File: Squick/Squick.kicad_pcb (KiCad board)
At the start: 2 copper layers, 92 x 92 mm, 103 parts, among them J1 BT, J10 D24V3F-5V, J2 DEBUG_UART, J3 PROG, J4 VL53L0X_L, J5 VL53L0X_F, J6 VL53L0X_R, J7 ENK_L, J8 ENK_R, J9 BATT, Q1 AO3407A, Q2 AO3407A, SW1 USER_BUT_1, SW2 USER_BUT_2, SW3 RESET, SW4 ON/OFF, T1 SFH-313FA, T2 SFH-313FA, T3 SFH-313FA, T4 SFH-313FA, T5 SFH-313FA, T6 SFH-313FA, U1 STM32F411RETx, U10 LM1117-3.3, U2 CD4051B, U3 KTIR0711S, U4 CD4051B, U5 KTIR0711S, U6 KTIR0711S, U7 KTIR0711S, U8 Adafruit_4554, U9 TB6612FNG

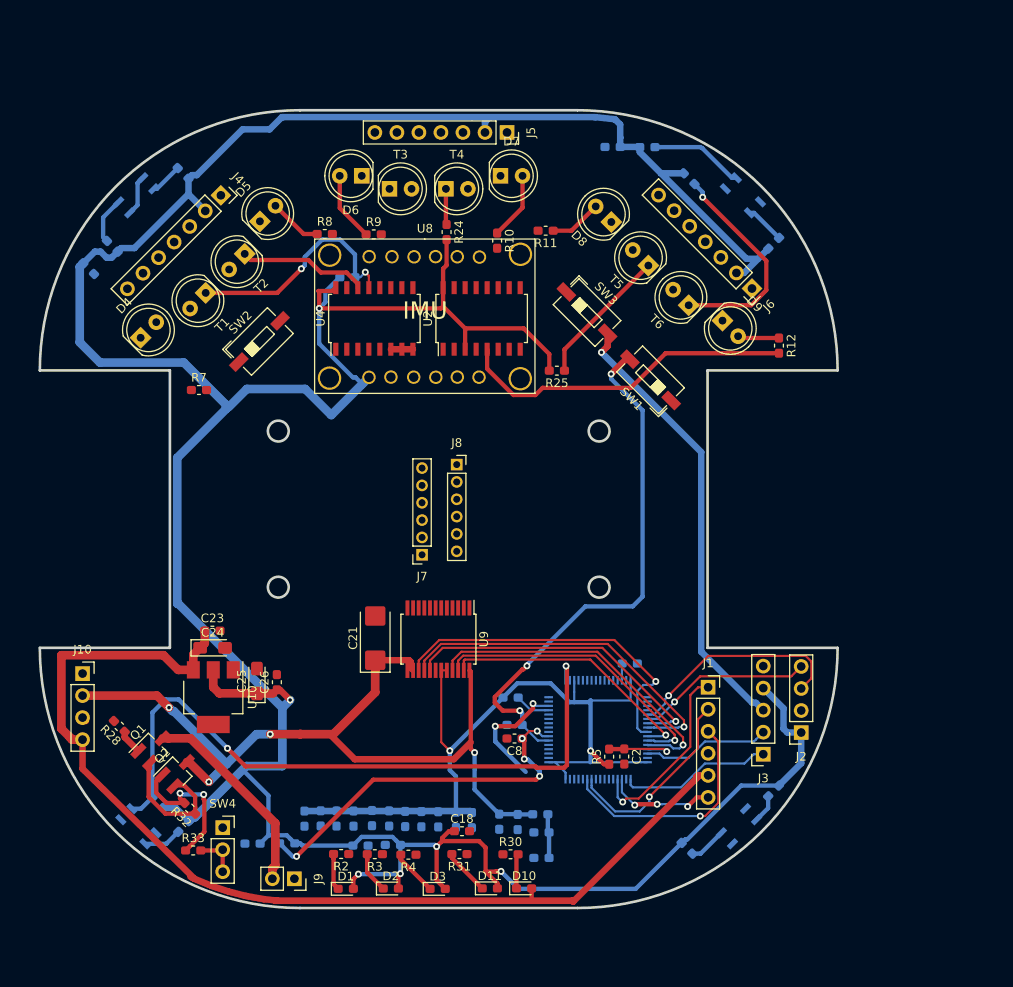
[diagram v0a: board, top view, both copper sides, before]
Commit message: Optimalization of connections and some reorganizations. Light in the tunnel
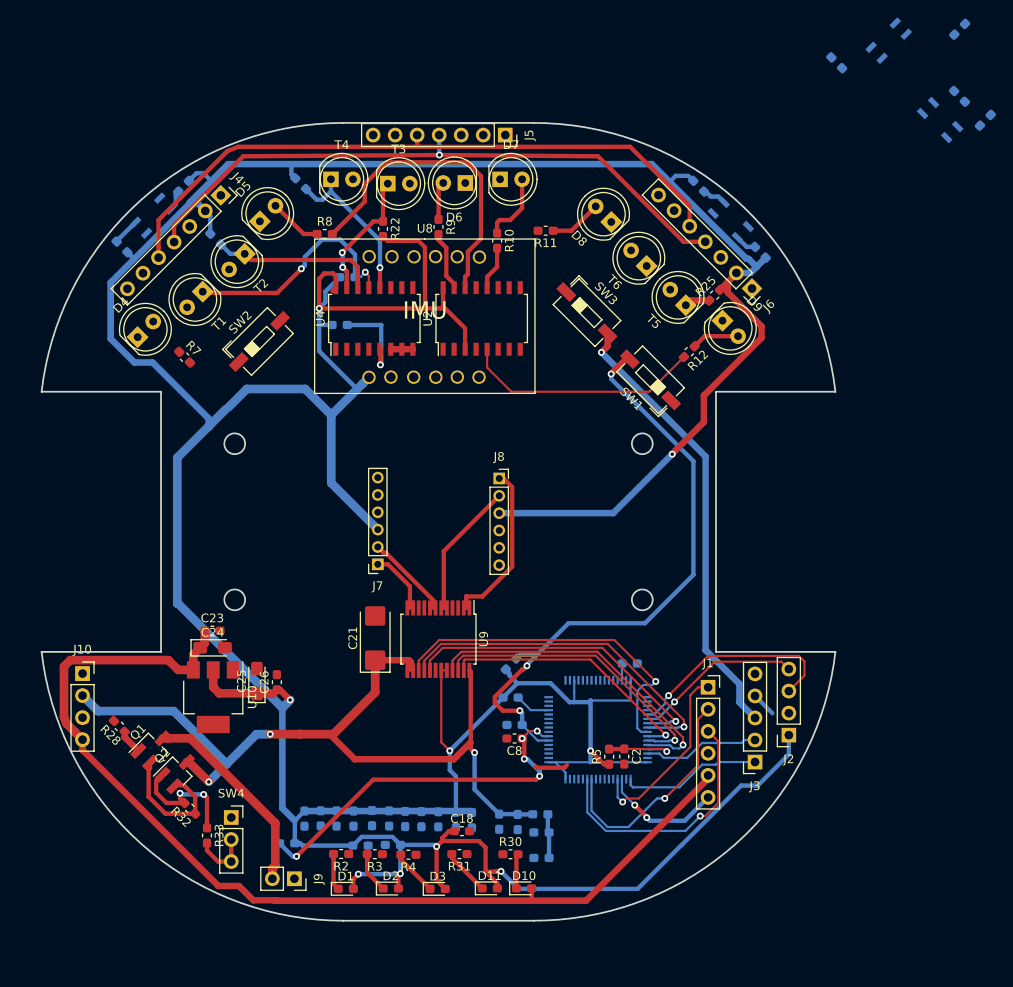
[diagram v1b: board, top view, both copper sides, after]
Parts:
- R22: moved to F.Cu
- R24: moved to B.Cu
- moved R18 123.2 mm to (243.2, 35.1)
- moved R19 123.2 mm to (240.2, 32.3)
- moved U6 123.2 mm to (237.9, 35.1)
- moved R23 92.2 mm to (226.0, 28.5)
- moved U7 92.2 mm to (232.0, 25.9)
- moved R21 90.4 mm to (240.2, 24.6)
- moved R26 43.7 mm to (168.7, 58.7), turned to 180 degrees
- moved R1 36.3 mm to (188.5, 97.8), turned to 45 degrees
- moved R22 28.1 mm to (173.7, 47.6), turned to 270 degrees
- moved R25 20.2 mm to (211.9, 55.3), turned to 45 degrees
- moved R24 17.7 mm to (164.2, 42.4), turned to 135 degrees
- moved R20 15.0 mm to (154.4, 48.8)
- moved T4 13.3 mm to (167.7, 41.9)
- moved D6 12.0 mm to (183.2, 42.3)
- moved R12 10.4 mm to (209.0, 61.8), turned to 225 degrees
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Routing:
- net SCL: track 0.00 -> 75.6 mm
- net KTIR_3: track 77.6 -> 3.82 mm, vias 2 -> 0
- net SDA: track 0.00 -> 72.9 mm, vias 0 -> 1
- net IR_2: track 0.00 -> 36.0 mm
- net +3.3V: track 512.5 -> 534.5 mm, vias 8 -> 9
- net M1_R: track 0.00 -> 19.8 mm
- net +5V: track 167.3 -> 148.0 mm
- net M2_R: track 0.00 -> 16.2 mm
- net PT_3: track 0.00 -> 15.3 mm, vias 0 -> 2
- net PT_4: track 4.14 -> 19.1 mm, vias 0 -> 1
- net PT_6: track 25.3 -> 10.4 mm
- net V_batt: track 19.5 -> 5.09 mm, vias 2 -> 0
- net PT_5: track 16.1 -> 2.93 mm
- net IR_6: track 39.6 -> 28.1 mm
- net M2_L: track 0.00 -> 10.5 mm
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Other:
- board size 92 x 92 mm -> 91.5 x 92 mm

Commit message: Almost finished. It's getting really tight
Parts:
- C8: moved to B.Cu
- moved C19 23.1 mm to (164.5, 110.9)
- moved C20 23.1 mm to (166.7, 110.9)
- moved R29 23.1 mm to (169.4, 112.1)
- moved R27 23.1 mm to (169.3, 110.0)
- moved C22 20.6 mm to (173.0, 112.1), turned to 180 degrees
- moved C23 3.23 mm to (150.8, 94.0)
- moved C1 2.14 mm to (188.7, 107.0)
- moved C24 1.85 mm to (152.2, 95.8)
- moved D6 1.25 mm to (183.9, 43.3)
- moved D7 1.25 mm to (187.9, 42.9)
- moved T3 1.25 mm to (175.0, 43.4)
- moved T4 1.25 mm to (168.4, 42.9)
- moved J10 1.01 mm to (139.9, 99.5)
- moved C8 0.96 mm to (188.7, 105.5)
- moved R24 0.81 mm to (163.9, 43.1)
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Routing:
- net MISO: track 0.24 -> 104.4 mm, vias 0 -> 2
- net IMU_CS: track 0.00 -> 103.0 mm, vias 0 -> 2
- net IR_A: track 0.00 -> 83.9 mm, vias 0 -> 3
- net IR_B: track 0.00 -> 79.2 mm, vias 0 -> 3
- net SCK: track 0.28 -> 77.7 mm, vias 0 -> 4
- net IMU_INT: track 0.00 -> 75.8 mm, vias 0 -> 2
- net VL_XSHUT: track 0.00 -> 75.6 mm, vias 0 -> 2
- net IR_C: track 0.00 -> 73.4 mm, vias 0 -> 3
- net MOSI: track 0.00 -> 70.6 mm, vias 0 -> 2
- net BUT_2: track 9.10 -> 75.7 mm, vias 1 -> 3
- net VL_INT_R: track 0.00 -> 64.6 mm, vias 0 -> 3
- net +3.3V: track 534.5 -> 587.1 mm, vias 9 -> 10
- net IR_1: track 0.00 -> 37.2 mm
- net +5V: track 148.0 -> 121.2 mm
- net BT_RX: track 26.6 -> 47.1 mm
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
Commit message: Everything connected
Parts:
- moved R18 79.5 mm to (163.8, 38.9), turned to 45 degrees
- moved U6 69.5 mm to (168.5, 38.8), turned to 270 degrees
- moved R19 66.4 mm to (174.1, 39.4), turned to 0 degrees
- moved R21 54.2 mm to (187.9, 38.6), turned to 0 degrees
- moved U7 41.7 mm to (192.3, 38.5), turned to 270 degrees
- moved R1 41.5 mm to (206.3, 60.3), turned to 135 degrees
- moved R23 30.5 mm to (197.5, 39.4), turned to 0 degrees
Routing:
- net KTIR_3: track 0.00 -> 145.4 mm, vias 0 -> 10
- net VL_INT_L: track 0.05 -> 112.9 mm, vias 0 -> 5
- net SDA: track 73.1 -> 182.8 mm, vias 1 -> 9
- net KTIR_4: track 0.00 -> 107.0 mm, vias 0 -> 4
- net VL_INT_F: track 0.00 -> 99.4 mm, vias 0 -> 8
- net SCL: track 75.8 -> 170.2 mm, vias 0 -> 6
- net LED_2: track 0.00 -> 80.2 mm, vias 0 -> 5
- net PT_MEAS: track 0.00 -> 79.1 mm, vias 0 -> 3
- net PT_A: track 5.42 -> 77.8 mm, vias 2 -> 5
- net PT_B: track 0.00 -> 66.2 mm, vias 0 -> 5
- net PT_C: track 0.00 -> 63.5 mm, vias 0 -> 5
- net PT_5: track 2.93 -> 64.8 mm, vias 0 -> 2
- net LED_3: track 0.00 -> 60.7 mm, vias 0 -> 3
- net LED_1: track 0.00 -> 58.4 mm, vias 0 -> 4
- net BUT_2: track 75.7 -> 126.9 mm, vias 3 -> 9
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
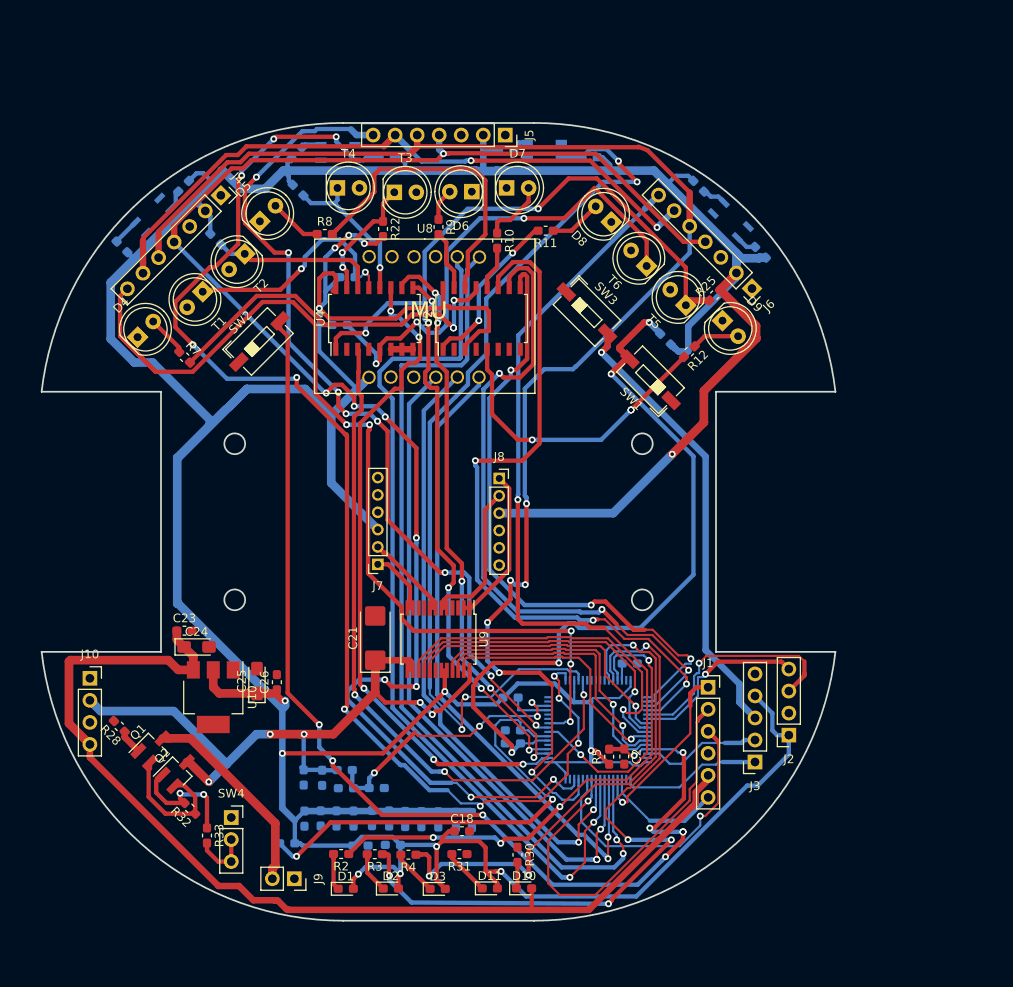
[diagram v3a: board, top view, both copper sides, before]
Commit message: Improved via drills and added graphic symbols
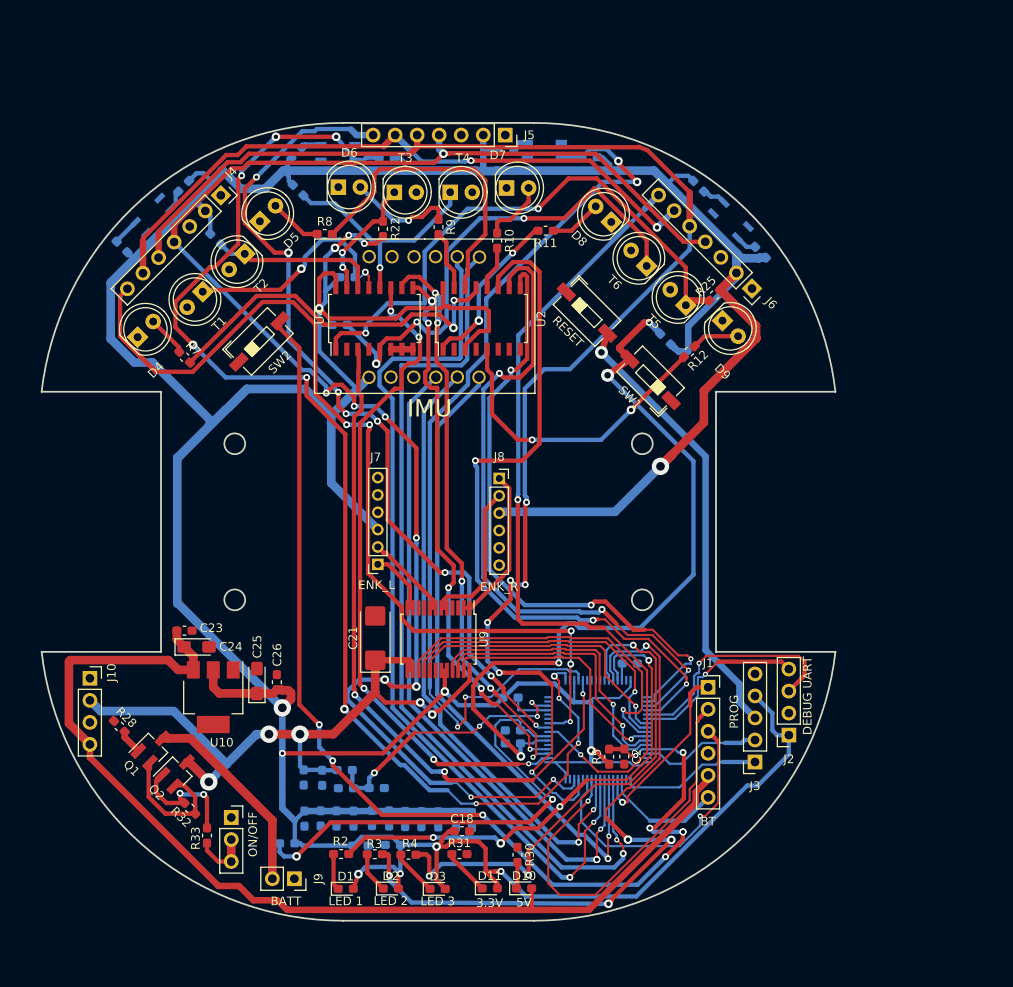
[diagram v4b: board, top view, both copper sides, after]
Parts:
- added G***: LOGO, graphics:Mouse_20x20mm, B.Cu at (163.8, 81.3)
- D1: value LED_1 -> LED 1
- D10: value LED_5V -> 5V
- D11: value LED_3.3V -> 3.3V
- D2: value LED_2 -> LED 2
- D3: value LED_3 -> LED 3
- J2: value DEBUG_UART -> DEBUG UART
- moved D6 15.4 mm to (168.6, 42.8), turned to 0 degrees
- moved T4 13.0 mm to (181.4, 43.4)
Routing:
- net PT_4: track 18.8 -> 28.1 mm
- net Net-(D6-Pad2): track 3.74 -> 12.5 mm, vias 0 -> 1
- net +3.3V: track 607.8 -> 613.8 mm
- net IR_1: track 43.6 -> 45.2 mm, vias 3 -> 2
- net BUT_1: track 86.1 -> 87.6 mm
- net Vin: track 77.7 -> 79.0 mm
- net PT_6: track 57.9 -> 59.1 mm
- net V_batt: track 31.9 -> 32.6 mm
- net KTIR_4: track 107.0 -> 106.5 mm
- net IR_6: vias 3 -> 2
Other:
- board text added: "Patryk Szydlik"
- board text added: "Piotr Gorzelnik"
- board text added: "Squick"

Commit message: Made more space for BT module and 5V converter
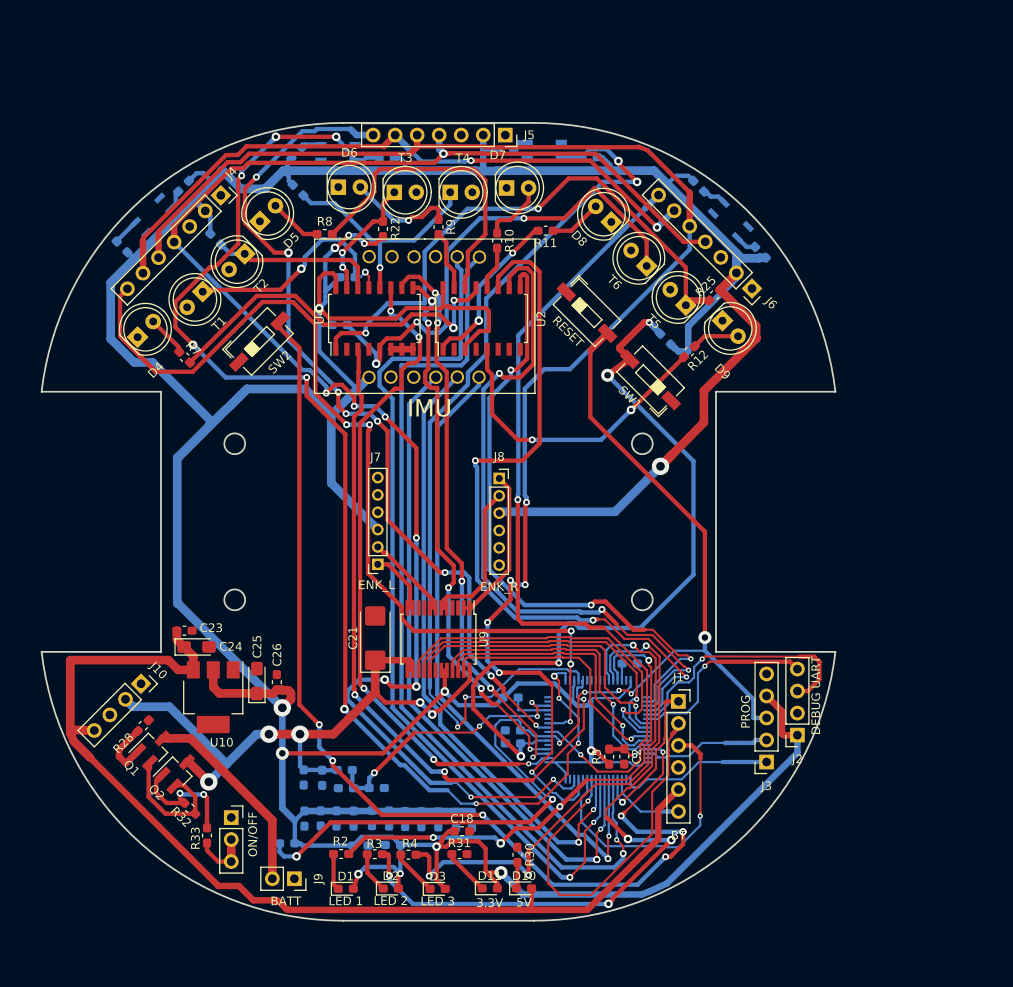
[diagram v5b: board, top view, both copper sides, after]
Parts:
- moved J10 5.93 mm to (145.8, 100.1), turned to 315 degrees
- moved G*** 5.10 mm to (159.0, 79.8), turned to 180 degrees
- moved J1 3.79 mm to (207.8, 102.1)
- moved R28 2.76 mm to (146.1, 104.9), turned to 45 degrees
- moved J3 1.33 mm to (217.9, 109.1)
- moved J2 0.99 mm to (221.5, 106.0)
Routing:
- net RESET: track 106.4 -> 134.3 mm, vias 3 -> 7
- net BT_EN: track 14.0 -> 8.99 mm
- net Net-(Q1-Pad1): track 2.86 -> 6.97 mm
- net Vin: track 79.0 -> 74.9 mm
- net BT_State: track 21.4 -> 17.7 mm
- net BT_RX: track 47.0 -> 43.7 mm
- net DEBUG_RX: track 27.2 -> 29.5 mm
- net IR_B: track 79.1 -> 80.9 mm
- net DEBUG_TX: track 20.6 -> 22.3 mm
- net SYS_SWCLCK: track 16.4 -> 17.7 mm
- net BT_TX: track 33.7 -> 32.4 mm
- net PT_MEAS: track 79.5 -> 80.5 mm
- net L_IN1: track 33.2 -> 34.0 mm
- net +3.3V: track 613.8 -> 614.6 mm
- net SYS_SWDIO: track 14.0 -> 14.8 mm
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
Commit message: PCB project done
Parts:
- moved Q2 0.92 mm to (149.5, 110.9)
- moved Q1 0.92 mm to (146.7, 108.2)
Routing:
- net KTIR_2: track 2.51 -> 168.8 mm, vias 0 -> 12
- net KTIR_1: track 2.38 -> 116.9 mm, vias 0 -> 6
- net VL_XSHUT: track 75.5 -> 159.8 mm, vias 2 -> 9
- net M2_R: track 17.9 -> 0.65 mm
- net +3.3V: track 614.6 -> 620.1 mm
- net VL_INT_L: track 112.9 -> 115.8 mm
- net Net-(Q2-Pad1): track 14.3 -> 11.3 mm
- net KTIR_4: track 106.5 -> 103.6 mm
- net Net-(Q1-Pad2): track 15.2 -> 12.7 mm
- net V_batt: track 32.6 -> 30.2 mm
- net VCC: track 23.3 -> 24.9 mm
- net IR_2: track 35.8 -> 34.2 mm
- net Vin: track 74.9 -> 76.4 mm
- net M1_R: track 18.4 -> 19.7 mm
- net PT_5: track 64.8 -> 66.1 mm
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- added copper zone on F.Cu, net +3.3V
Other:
- net class gruby added: clearance 0.2, trace_width 2, via_dia 0.8, via_drill 0.4

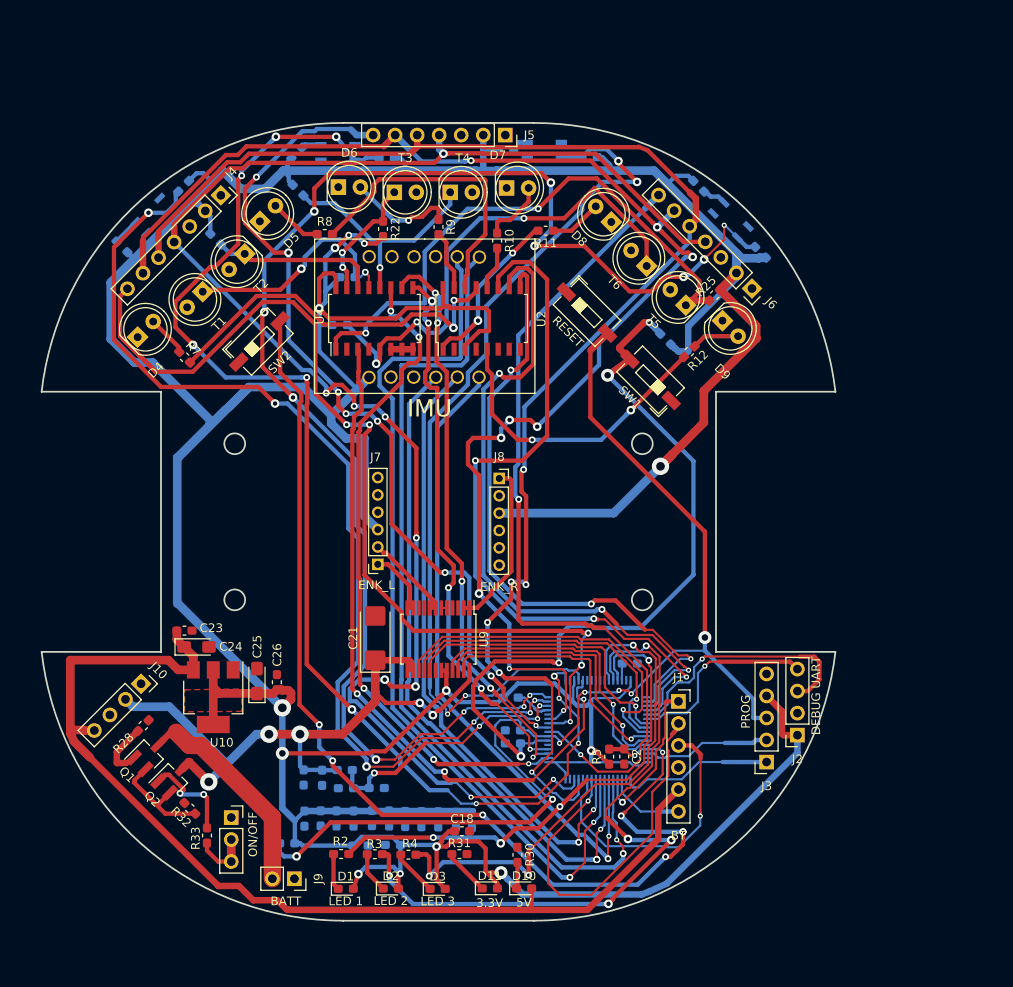
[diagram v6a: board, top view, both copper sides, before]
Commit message: Created GND planes
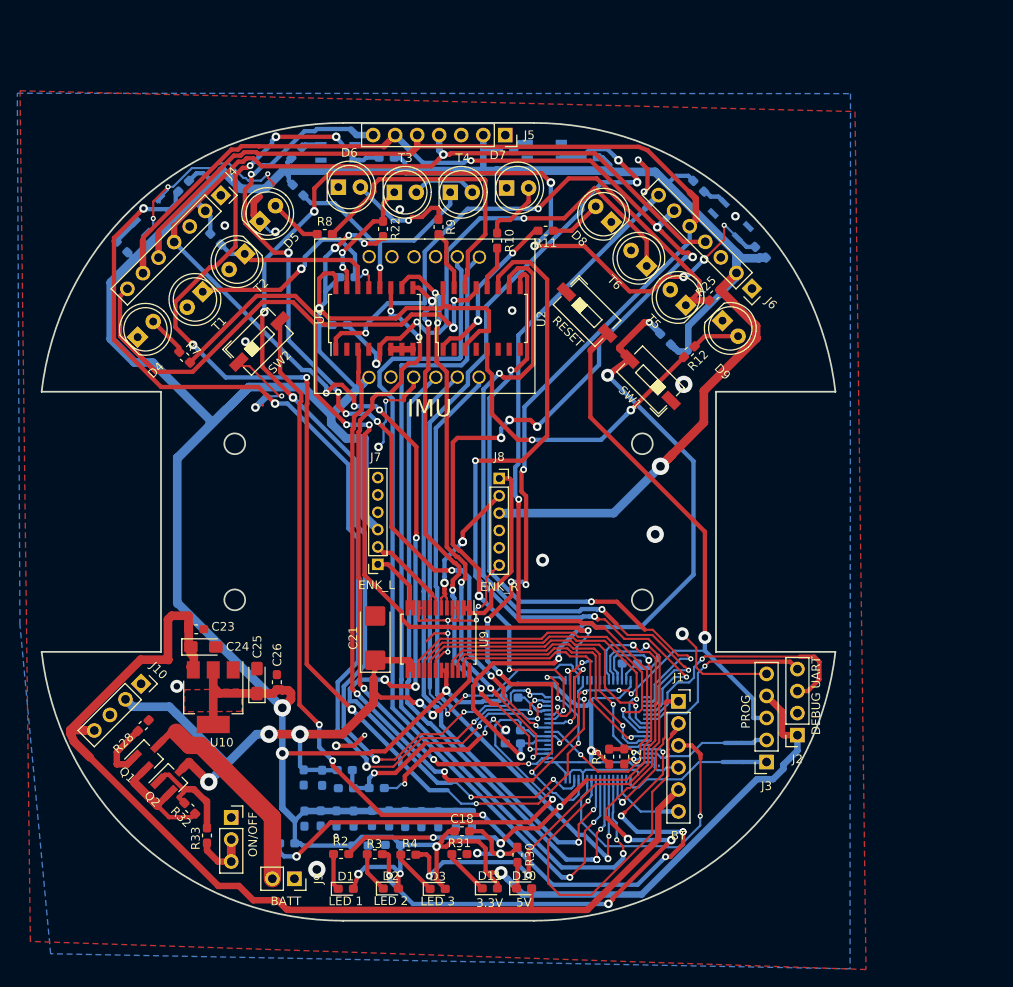
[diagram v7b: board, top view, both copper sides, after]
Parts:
- moved C23 1.37 mm to (152.2, 93.8)
- moved C24 0.78 mm to (153.0, 95.8)
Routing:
- net GND: track 3.58 -> 183.6 mm, vias 0 -> 40
- net M2_R: track 0.65 -> 17.5 mm, vias 0 -> 3
- net Net-(Q1-Pad2): track 12.7 -> 18.0 mm
- net Net-(Q1-Pad1): track 5.79 -> 8.41 mm
- net VL_INT_L: track 115.8 -> 118.0 mm
- net VL_XSHUT: track 159.8 -> 161.9 mm
- net M2_L: track 10.5 -> 12.1 mm
- net Net-(Q2-Pad1): track 11.3 -> 12.7 mm, vias 2 -> 0
- net M1_R: track 19.7 -> 21.0 mm
- net BUT_1: track 87.3 -> 86.1 mm
- net KTIR_3: track 145.5 -> 146.5 mm
- net +5V: track 120.7 -> 121.6 mm
- net KTIR_1: track 116.9 -> 117.8 mm
- net KTIR_2: track 168.8 -> 169.7 mm
- net PT_A: track 77.5 -> 78.4 mm
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- added copper zone on B.Cu, net GND
- added copper zone on F.Cu, net GND
